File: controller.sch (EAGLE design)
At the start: 40 parts, among them IC1 7805DT, Q3 MOSFET-NCHANNELFDD8780, Q5 MMBT4403, U1 ATMEGA328P, Y1 16MHz

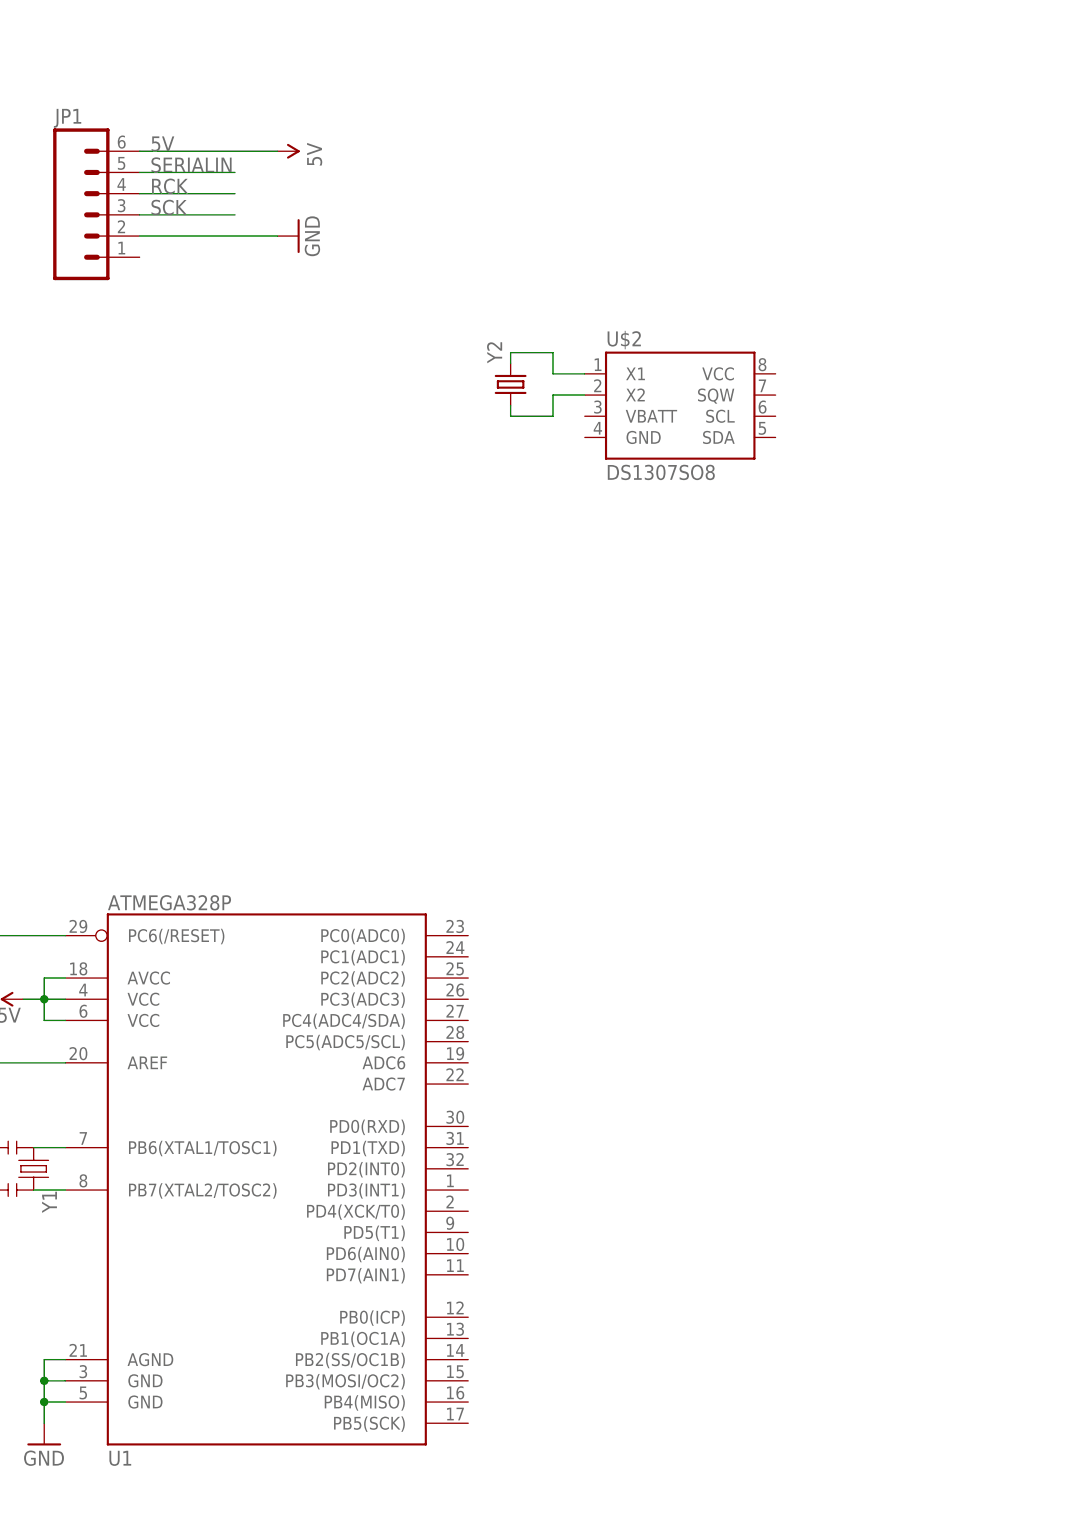
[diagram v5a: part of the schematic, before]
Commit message: completed RTC and micro schematic. to do: switches
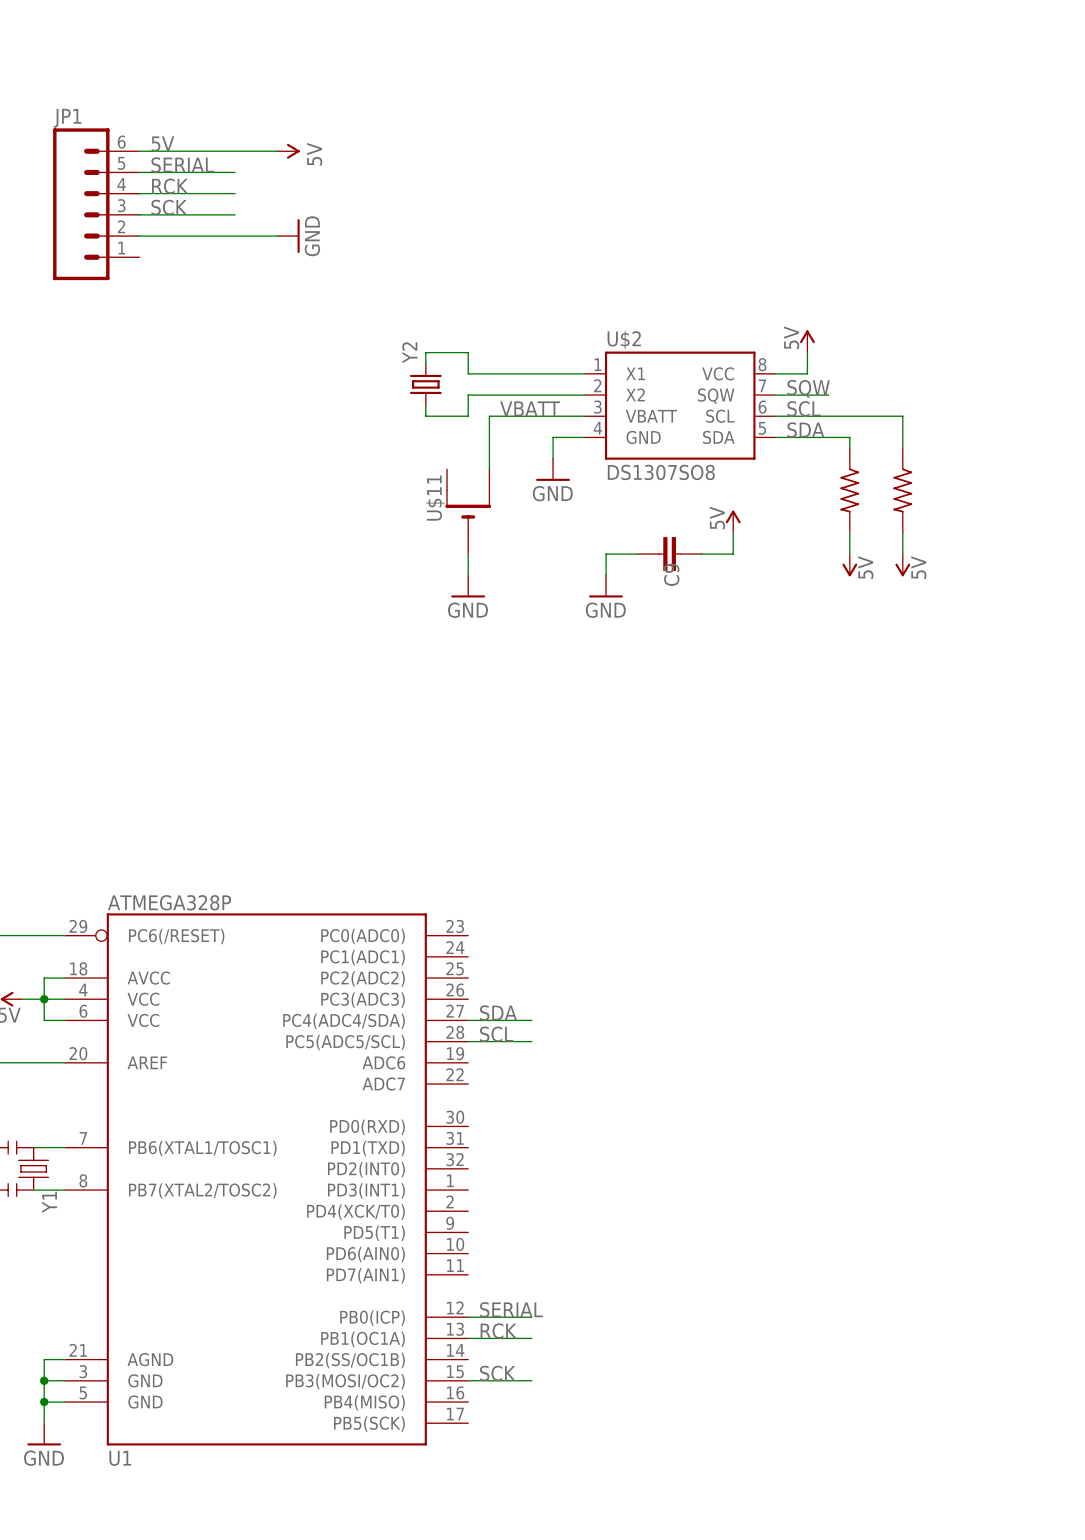
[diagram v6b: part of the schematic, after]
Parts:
- added C9: (no value), SparkFun-Capacitors:CAP0805
- added U$10, U$9: (no value), jt_parts:RESISTOR
- added U$11: (no value), adafruit:CR1220THM
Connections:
- removed net SERIALIN: JP1.5
- new net SCL: U$10.1, U$2.SCL, U1.PC5(ADC5/SCL)
- new net SDA: U$2.SDA, U$9.1, U1.PC4(ADC4/SDA)
- new net SERIAL: JP1.5, U1.PB0(ICP)
- new net SQW: U$2.SQW
- new net VBATT: U$11.+1, U$2.VBATT
- net 5V: now also C9.1, U$10.2, U$2.VCC, U$9.2
- net GND: now also C9.2, U$11.-, U$2.GND
- net RCK: now also U1.PB1(OC1A)
- net SCK: now also U1.PB3(MOSI/OC2)
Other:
- moved on the sheet: Y2
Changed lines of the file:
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@@
 <part name="U$8" library="jt_parts" deviceset="RESISTOR" device=""/>
 <part name="SUPPLY5" library="SparkFun-Aesthetics" deviceset="5V" device=""/>
+<part name="GND12" library="SparkFun-Aesthetics" deviceset="GND" device=""/>
+<part name="C9" library="SparkFun-Capacitors" deviceset="CAP" device="0805"/>
+<part name="SUPPLY6" library="SparkFun-Aesthetics" deviceset="5V" device=""/>
+<part name="SUPPLY7" library="SparkFun-Aesthetics" deviceset="5V" device=""/>
+<part name="GND13" library="SparkFun-Aesthetics" deviceset="GND" device=""/>
+<part name="U$9" library="jt_parts" deviceset="RESISTOR" device=""/>
+<part name="U$10" library="jt_parts" deviceset="RESISTOR" device=""/>
+<part name="SUPPLY8" library="SparkFun-Aesthetics" deviceset="5V" device=""/>
+<part name="SUPPLY9" library="SparkFun-Aesthetics" deviceset="5V" device=""/>
+<part name="U$11" library="adafruit" deviceset="CR1220" device="THM"/>
+<part name="GND14" library="SparkFun-Aesthetics" deviceset="GND" device=""/>
 </parts>
 <sheets>
@@
 <instance part="Y1" gate="G$1" x="64.77" y="146.05" rot="R270"/>
 <instance part="GND" gate="1" x="52.07" y="139.7"/>
-<instance part="Y2" gate="G$1" x="121.92" y="240.03" rot="R90"/>
+<instance part="Y2" gate="G$1" x="111.76" y="240.03" rot="R90"/>
 <instance part="S1" gate="1" x="322.58" y="116.84"/>
 <instance part="12V_IN" gate="G$1" x="306.07" y="114.3" smashed="yes">
@@
 <attribute name="VALUE" x="37.084" y="189.484" size="1.778" layer="96" rot="R90"/>
 </instance>
+<instance part="GND12" gate="1" x="127" y="228.6"/>
+<instance part="C9" gate="G$1" x="139.7" y="219.71" smashed="yes" rot="R270">
+<attribute name="NAME" x="140.335" y="218.694" size="1.778" layer="95" rot="R270"/>
+<attribute name="VALUE" x="135.509" y="218.694" size="1.778" layer="96" rot="R270"/>
+</instance>
+<instance part="SUPPLY6" gate="G$1" x="157.48" y="243.84" smashed="yes">
+<attribute name="VALUE" x="156.464" y="244.094" size="1.778" layer="96" rot="R90"/>
+</instance>
+<instance part="SUPPLY7" gate="G$1" x="148.59" y="222.25" smashed="yes">
+<attribute name="VALUE" x="147.574" y="222.504" size="1.778" layer="96" rot="R90"/>
+</instance>
+<instance part="GND13" gate="1" x="133.35" y="214.63"/>
+<instance part="U$9" gate="G$1" x="162.56" y="227.33" smashed="yes" rot="R270">
+<attribute name="VALUE" x="159.258" y="231.14" size="1.778" layer="96" rot="R270"/>
+</instance>
+<instance part="U$10" gate="G$1" x="168.91" y="227.33" smashed="yes" rot="R270">
+<attribute name="VALUE" x="165.608" y="231.14" size="1.778" layer="96" rot="R270"/>
+</instance>
+<instance part="SUPPLY8" gate="G$1" x="162.56" y="219.71" smashed="yes" rot="R180">
+<attribute name="VALUE" x="163.576" y="219.456" size="1.778" layer="96" rot="R270"/>
+</instance>
+<instance part="SUPPLY9" gate="G$1" x="168.91" y="219.71" smashed="yes" rot="R180">
+<attribute name="VALUE" x="169.926" y="219.456" size="1.778" layer="96" rot="R270"/>
+</instance>
+<instance part="U$11" gate="G$1" x="116.84" y="224.79" rot="R90"/>
+<instance part="GND14" gate="1" x="116.84" y="214.63"/>
 </instances>
 <busses>
@@
 <pinref part="GND11" gate="1" pin="GND"/>
 </segment>
+<segment>
+<pinref part="U$2" gate="G$1" pin="GND"/>
+<wire x1="130.81" y1="233.68" x2="127" y2="233.68" width="0.1524" layer="91"/>
+<pinref part="GND12" gate="1" pin="GND"/>
+<wire x1="127" y1="233.68" x2="127" y2="231.14" width="0.1524" layer="91"/>
+</segment>
+<segment>
+<pinref part="C9" gate="G$1" pin="2"/>
+<wire x1="137.16" y1="219.71" x2="133.35" y2="219.71" width="0.1524" layer="91"/>
+<wire x1="133.35" y1="219.71" x2="133.35" y2="217.17" width="0.1524" layer="91"/>
+<pinref part="GND13" gate="1" pin="GND"/>
+</segment>
+<segment>
+<pinref part="GND14" gate="1" pin="GND"/>
+<pinref part="U$11" gate="G$1" pin="-"/>
+<wire x1="116.84" y1="217.17" x2="116.84" y2="219.71" width="0.1524" layer="91"/>
+</segment>
 </net>
 <net name="RCK" class="0">
@@
 <label x="78.74" y="262.89" size="1.778" layer="95"/>
 </segment>
+<segment>
+<pinref part="U1" gate="G$1" pin="PB1(OC1A)"/>
+<wire x1="116.84" y1="125.73" x2="124.46" y2="125.73" width="0.1524" layer="91"/>
+<label x="118.11" y="125.73" size="1.778" layer="95"/>
+</segment>
 </net>
 <net name="SCK" class="0">
@@
 <wire x1="77.47" y1="260.35" x2="88.9" y2="260.35" width="0.1524" layer="91"/>
 <label x="78.74" y="260.35" size="1.778" layer="95"/>
+</segment>
+<segment>
+<pinref part="U1" gate="G$1" pin="PB3(MOSI/OC2)"/>
+<wire x1="116.84" y1="120.65" x2="124.46" y2="120.65" width="0.1524" layer="91"/>
+<label x="118.11" y="120.65" size="1.778" layer="95"/>
 </segment>
 </net>
@@
 <wire x1="38.1" y1="189.23" x2="38.1" y2="186.69" width="0.1524" layer="91"/>
 </segment>
-</net>
-<net name="SERIALIN" class="0">
+<segment>
+<pinref part="C9" gate="G$1" pin="1"/>
+<wire x1="144.78" y1="219.71" x2="148.59" y2="219.71" width="0.1524" layer="91"/>
+<wire x1="148.59" y1="219.71" x2="148.59" y2="222.25" width="0.1524" layer="91"/>
+<pinref part="SUPPLY7" gate="G$1" pin="5V"/>
+</segment>
+<segment>
+<pinref part="U$2" gate="G$1" pin="VCC"/>
+<wire x1="153.67" y1="241.3" x2="157.48" y2="241.3" width="0.1524" layer="91"/>
+<wire x1="157.48" y1="241.3" x2="157.48" y2="243.84" width="0.1524" layer="91"/>
+<pinref part="SUPPLY6" gate="G$1" pin="5V"/>
+</segment>
+<segment>
+<pinref part="U$9" gate="G$1" pin="2"/>
+<pinref part="SUPPLY8" gate="G$1" pin="5V"/>
+<wire x1="162.56" y1="222.25" x2="162.56" y2="219.71" width="0.1524" layer="91"/>
+</segment>
+<segment>
+<pinref part="SUPPLY9" gate="G$1" pin="5V"/>
+<pinref part="U$10" gate="G$1" pin="2"/>
+<wire x1="168.91" y1="219.71" x2="168.91" y2="222.25" width="0.1524" layer="91"/>
+</segment>
+</net>
+<net name="SERIAL" class="0">
 <segment>
 <pinref part="JP1" gate="G$1" pin="5"/>
 <wire x1="77.47" y1="265.43" x2="88.9" y2="265.43" width="0.1524" layer="91"/>
 <label x="78.74" y="265.43" size="1.778" layer="95"/>
+</segment>
+<segment>
+<pinref part="U1" gate="G$1" pin="PB0(ICP)"/>
+<wire x1="116.84" y1="128.27" x2="124.46" y2="128.27" width="0.1524" layer="91"/>
+<label x="118.11" y="128.27" size="1.778" layer="95"/>
 </segment>
 </net>
@@
 <segment>
 <pinref part="U$2" gate="G$1" pin="X1"/>
-<wire x1="130.81" y1="241.3" x2="127" y2="241.3" width="0.1524" layer="91"/>
-<wire x1="127" y1="241.3" x2="127" y2="243.84" width="0.1524" layer="91"/>
-<wire x1="127" y1="243.84" x2="121.92" y2="243.84" width="0.1524" layer="91"/>
+<wire x1="130.81" y1="241.3" x2="116.84" y2="241.3" width="0.1524" layer="91"/>
+<wire x1="116.84" y1="241.3" x2="116.84" y2="243.84" width="0.1524" layer="91"/>
+<wire x1="116.84" y1="243.84" x2="111.76" y2="243.84" width="0.1524" layer="91"/>
 <pinref part="Y2" gate="G$1" pin="2"/>
-<wire x1="121.92" y1="243.84" x2="121.92" y2="242.57" width="0.1524" layer="91"/>
+<wire x1="111.76" y1="243.84" x2="111.76" y2="242.57" width="0.1524" layer="91"/>
 </segment>
 </net>
@@
 <segment>
 <pinref part="U$2" gate="G$1" pin="X2"/>
-<wire x1="130.81" y1="238.76" x2="127" y2="238.76" width="0.1524" layer="91"/>
-<wire x1="127" y1="238.76" x2="127" y2="236.22" width="0.1524" layer="91"/>
-<wire x1="127" y1="236.22" x2="121.92" y2="236.22" width="0.1524" layer="91"/>
+<wire x1="130.81" y1="238.76" x2="116.84" y2="238.76" width="0.1524" layer="91"/>
+<wire x1="116.84" y1="238.76" x2="116.84" y2="236.22" width="0.1524" layer="91"/>
+<wire x1="116.84" y1="236.22" x2="111.76" y2="236.22" width="0.1524" layer="91"/>
 <pinref part="Y2" gate="G$1" pin="1"/>
-<wire x1="121.92" y1="236.22" x2="121.92" y2="237.49" width="0.1524" layer="91"/>
+<wire x1="111.76" y1="236.22" x2="111.76" y2="237.49" width="0.1524" layer="91"/>
 </segment>
 </net>
@@
 </segment>
 </net>
+<net name="VBATT" class="0">
+<segment>
+<pinref part="U$2" gate="G$1" pin="VBATT"/>
+<wire x1="130.81" y1="236.22" x2="119.38" y2="236.22" width="0.1524" layer="91"/>
+<label x="120.65" y="236.22" size="1.778" layer="95"/>
+<pinref part="U$11" gate="G$1" pin="+1"/>
+<wire x1="119.38" y1="229.87" x2="119.38" y2="236.22" width="0.1524" layer="91"/>
+</segment>
+</net>
+<net name="SQW" class="0">
+<segment>
+<pinref part="U$2" gate="G$1" pin="SQW"/>
+<wire x1="153.67" y1="238.76" x2="160.02" y2="238.76" width="0.1524" layer="91"/>
+<label x="154.94" y="238.76" size="1.778" layer="95"/>
+</segment>
+</net>
+<net name="SCL" class="0">
+<segment>
+<pinref part="U$2" gate="G$1" pin="SCL"/>
+<label x="154.94" y="236.22" size="1.778" layer="95"/>
+<wire x1="153.67" y1="236.22" x2="168.91" y2="236.22" width="0.1524" layer="91"/>
+<pinref part="U$10" gate="G$1" pin="1"/>
+<wire x1="168.91" y1="236.22" x2="168.91" y2="232.41" width="0.1524" layer="91"/>
+</segment>
+<segment>
+<pinref part="U1" gate="G$1" pin="PC5(ADC5/SCL)"/>
+<wire x1="116.84" y1="161.29" x2="124.46" y2="161.29" width="0.1524" layer="91"/>
+<label x="118.11" y="161.29" size="1.778" layer="95"/>
+</segment>
+</net>
+<net name="SDA" class="0">
+<segment>
+<pinref part="U$2" gate="G$1" pin="SDA"/>
+<wire x1="153.67" y1="233.68" x2="162.56" y2="233.68" width="0.1524" layer="91"/>
+<label x="154.94" y="233.68" size="1.778" layer="95"/>
+<pinref part="U$9" gate="G$1" pin="1"/>
+<wire x1="162.56" y1="233.68" x2="162.56" y2="232.41" width="0.1524" layer="91"/>
+</segment>
+<segment>
+<pinref part="U1" gate="G$1" pin="PC4(ADC4/SDA)"/>
+<wire x1="116.84" y1="163.83" x2="124.46" y2="163.83" width="0.1524" layer="91"/>
+<label x="118.11" y="163.83" size="1.778" layer="95"/>
+</segment>
+</net>

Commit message: Beginning of new controller board layout.
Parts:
- removed FRAME1: FRAME-LEDGER, SparkFun-Aesthetics:FRAME-LEDGER
- removed S2: SWITCH-MOMENTARY-2SIDE_EZ, SparkFun-Electromechanical:SWITCH-MOMENTARY-2SIDE_EZ
- added FRAME2: FRAME-LETTER, SparkFun-Aesthetics:FRAME-LETTER
- added SW1: ROTARTY_ENCODER, SparkFun-Electromechanical:ROTARTY_ENCODER
- added U$12, U$14, U$15: (no value), jt_parts:RESISTOR
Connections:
- new net N$13: S3.1, U$12.1
- new net N$16: S4.1, U$14.1
- new net N$17: S5.1, U$15.1
- new net N$18: U1.PD2(INT0)
- new net N$19: U1.PD4(XCK/T0)
- new net N$20: U1.PD7(AIN1)
- net 5V: now also U$14.2, U$15.2; no longer U$7.1
- net GND: now also S3.2, S4.2, S5.2
- net RXI: now also U1.PD0(RXD)
- net TXO: now also U1.PD1(TXD)
- net VCC: now also U$12.2, U$7.1
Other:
- moved on the sheet: 12V_IN, C1, C2, C3, C4, C5, C6, C7, C8, C9, D1, D2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
